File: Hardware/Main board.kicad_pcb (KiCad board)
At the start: 4 copper layers, 66 x 45 mm, 152 parts, among them J1 ST1W008S4TR2000, J2 USB_C_Receptacle_USB2.0, J4 USB_C_Receptacle_USB2.0, J5 7788, J6 7788, Q1 BUK9M11-40EX, Q2 BSZ025N04LS, Q3 BSZ025N04LS, Q4 BUK9M11-40EX, Q5 BUK9M11-40EX, U1 ESP32-S3, U10 TPS55288QRPMRQ1, U11 DPS368, U12 TCMT1109, U2 SN65HVD230, U3 LM66200DRLR, U4 MAX77827AEFD+T, U5 SC4215ASTRT, U7 BU27006MUC-ZTR, U8 INA219AxDCN, U9 LM74810, Y1 R940000171

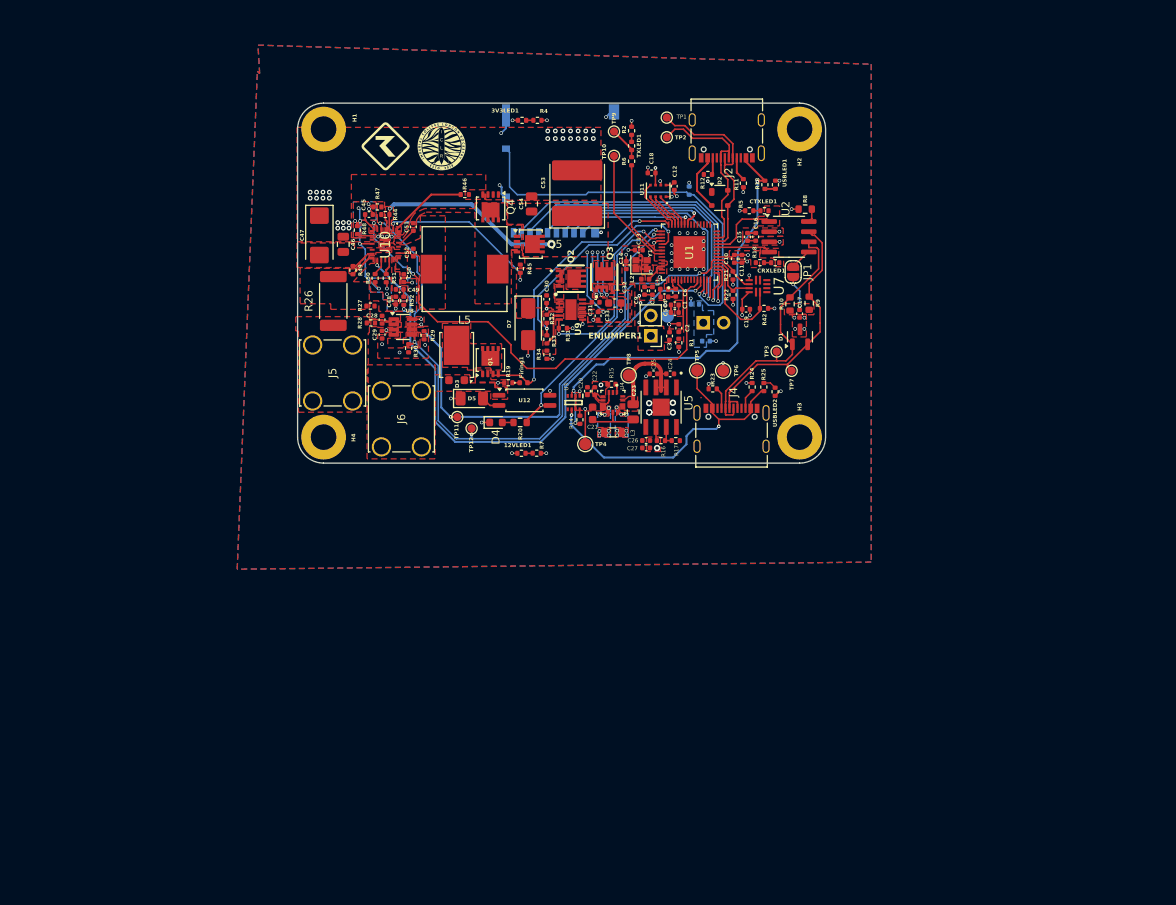
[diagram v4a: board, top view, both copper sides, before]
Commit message: Swapped battery & nichrome positions
fixed crystal and other small things
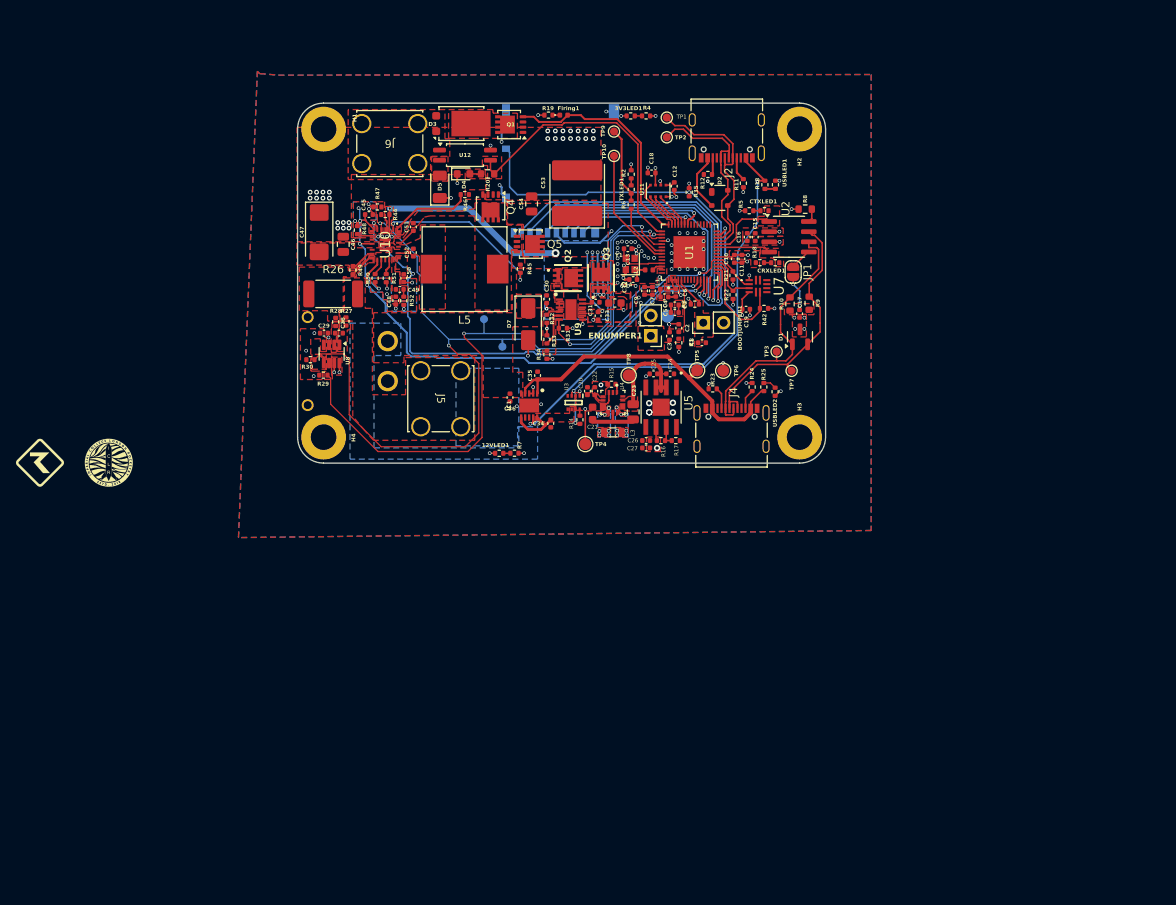
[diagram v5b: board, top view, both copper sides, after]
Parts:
- added C34: 40uF, Capacitor_SMD:C_0402_1005Metric, F.Cu at (111.3, 111.4)
- added C35: 1uF, Capacitor_SMD:C_0402_1005Metric, F.Cu at (109.7, 105.4)
- added C36: 1uF, Capacitor_SMD:C_0402_1005Metric, F.Cu at (106.2, 108.1)
- added IC1: LTC4413EDD#PBF, iclr:SON50P300X300X80-11N-D, F.Cu at (108.6, 109.1)
- added J3: XT30PW-M, iclr:XT30PWM, B.Cu at (85.0, 103.6)
- BOOTJUMPER1, C8, R3, R35: moved to F.Cu
- TP11, TP12: moved to B.Cu
- moved G*** 58.6 mm to (47.5, 116.3)
- moved G*** 57.4 mm to (56.1, 116.3)
- moved J6 35.7 mm to (94.7, 78.9), turned to 180 degrees
- moved Firing1 33.8 mm to (112.9, 72.8)
- moved R19 33.8 mm to (111.0, 72.8)
- moved U12 31.5 mm to (100.6, 77.8)
- moved D4 31.3 mm to (100.4, 80.2)
- moved R20 31.3 mm to (103.4, 80.2)
- moved Q1 29.7 mm to (106.3, 74.0), turned to 180 degrees
- moved D3 28.9 mm to (100.1, 73.9), turned to 90 degrees
- moved D5 26.8 mm to (97.4, 81.8), turned to 90 degrees
- moved J5 18.9 mm to (100.1, 104.8), turned to -90 degrees
- moved 3V3LED1 13.6 mm to (121.3, 72.9)
- moved R4 13.6 mm to (123.2, 72.9)
- moved R29 13.5 mm to (82.9, 105.3), turned to 0 degrees
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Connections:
- net /Voltage Regulation/VIN renamed Cell_+
- R26 pad 1: /Voltage Regulation/ISN_2 -> /PyroPWR
- R26 pad 2: /PyroPWR -> /Voltage Regulation/ISN_2
- R27 pad 1: /Voltage Regulation/ISN_2 -> /PyroPWR
- R28 pad 1: /PyroPWR -> /Voltage Regulation/ISN_2
- U1 pad 27: unconnected-(U1-GPIO21-Pad27) -> /Stat
- U3 pad 6: RBUS_uC_V -> /Power/RBUS + Cell
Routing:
- net /Stat: track 0.00 -> 46.3 mm, vias 0 -> 2
- net /SDA-CS: track 55.0 -> 79.3 mm
- net /SCL_I2C: track 88.4 -> 112.0 mm, vias 4 -> 3
- net /INT: track 68.5 -> 56.2 mm
- net /Nuke 1: track 37.5 -> 28.9 mm, vias 2 -> 0
- net +3V3: track 26.3 -> 33.3 mm, vias 21 -> 22
- net /Power/RBUS + Cell: track 0.00 -> 6.62 mm
- net Net-(U1-XTAL_N): track 0.00 -> 6.27 mm
- net Net-(U1-U0TXD/PROG/GPIO43): track 12.7 -> 7.29 mm
- net /TXD: track 4.11 -> 9.53 mm
- net /BOOT: track 0.46 -> 3.97 mm
- net /EN: track 24.9 -> 27.9 mm
- net Net-(C14-Pad1): track 0.00 -> 2.71 mm
- net /Cont 1: track 33.8 -> 36.3 mm, vias 2 -> 0
- net Net-(D5-A): track 2.35 -> 0.00 mm
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- added copper zone on F.Cu, net /BOOT
- added copper zone on F.Cu, net /Cont 1
- added copper zone on F.Cu, net /Power/RBUS + Cell
- added copper zone on B.Cu, net /PyroPWR
- added copper zone on B.Cu, net /Voltage Regulation/Switch_out
- added copper zone on B.Cu, net Cell_+
- added copper zone on F.Cu, net Net-(C6-Pad1)
- added copper zone on F.Cu, net Net-(D4-A)
- added copper zone on F.Cu, net Net-(D5-A)
- removed copper zone on B.Cu, net /BOOT
- removed copper zone on F.Cu, net Net-(C14-Pad1)
- removed copper zone on F.Cu, net Net-(U1-XTAL_N)
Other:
- board text removed: "C46"

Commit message: Applied more review suggestions
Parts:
- C23: footprint Capacitor_SMD:C_0805_2012Metric -> Capacitor_SMD:C_0603_1608Metric
- moved CRXLED1 2.20 mm to (137.2, 91.3), turned to 0 degrees
- moved CTXLED1 2.11 mm to (135.9, 84.9), turned to 0 degrees
- moved R5 1.69 mm to (137.8, 84.9), turned to 180 degrees
- moved R18 1.62 mm to (139.1, 91.3), turned to 180 degrees
- moved U2 1.18 mm to (139.9, 88.1)
- moved C15 0.96 mm to (135.9, 88.1)
- moved C16 0.96 mm to (134.9, 88.1)
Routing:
- net /CAN_TX: track 8.89 -> 0.00 mm
- net /CAN_RX: track 6.77 -> 0.00 mm
- net /SDA-BuckBC: track 60.2 -> 57.3 mm, vias 3 -> 2
- net +3V3: track 33.3 -> 31.1 mm, vias 22 -> 28
- net /CAN-: track 33.9 -> 35.4 mm
- net /INT: track 56.2 -> 54.7 mm
- net Cell_+: track 0.50 -> 1.91 mm
- net /CAN+: track 34.7 -> 35.9 mm
- net GND: track 49.8 -> 48.7 mm, vias 125 -> 126
- net Net-(U10-DR1H): track 21.2 -> 20.4 mm
- net /CAN-BUS/Vref: track 2.71 -> 2.15 mm
- net AGND: track 19.6 -> 20.1 mm
- net Net-(U2-Rs): track 1.71 -> 2.21 mm
